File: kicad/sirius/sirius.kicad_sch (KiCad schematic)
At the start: 59 parts, among them J1 IPEX_MHF1, J2 Power In, J3 Screw_Terminal, Q1 Q_PMOS_GSD, Q2 Q_NMOS_GSD, Q3 Q_NMOS_GSD, U1 Power_Connector, U2 AP63301WU-7, U3 RFM95W-915S2, U4 LC29H (DA), U5 Pi Zero 2W

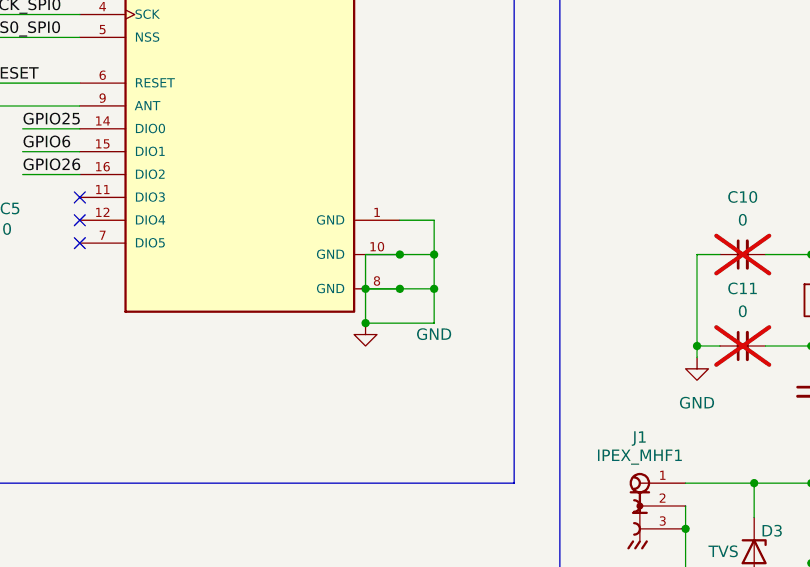
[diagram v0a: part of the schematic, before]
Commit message: Finish Sopdet schematic
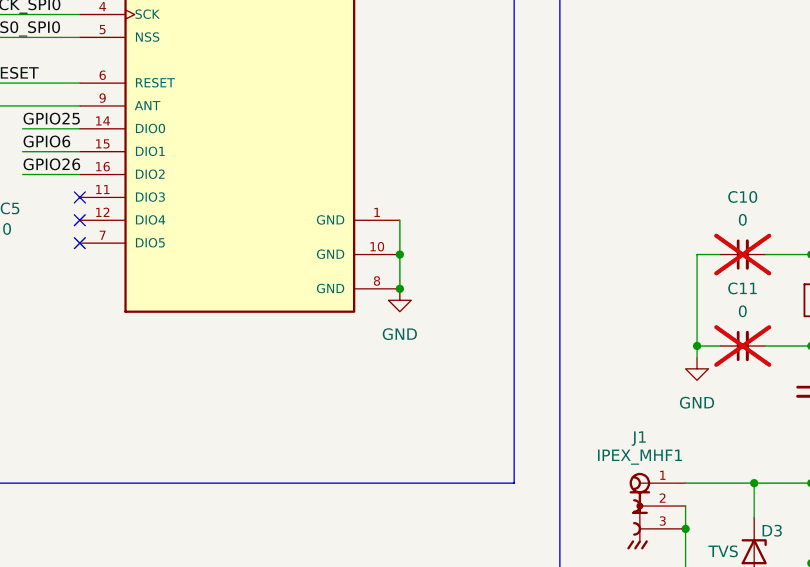
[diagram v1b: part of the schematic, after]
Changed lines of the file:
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@@
 	)
 	(junction
-		(at 74.93 184.15)
-		(diameter 0)
-		(color 0 0 0 0)
-	)
-	(junction
 		(at 196.85 198.12)
 		(diameter 0)
@@
 	)
 	(junction
-		(at 82.55 184.15)
+		(at 180.34 137.16)
 		(diameter 0)
 		(color 0 0 0 0)
 	)
 	(junction
-		(at 180.34 137.16)
+		(at 383.54 199.39)
 		(diameter 0)
 		(color 0 0 0 0)
 	)
 	(junction
-		(at 383.54 199.39)
+		(at 36.83 64.77)
 		(diameter 0)
 		(color 0 0 0 0)
 	)
 	(junction
-		(at 36.83 64.77)
+		(at 78.74 184.15)
 		(diameter 0)
 		(color 0 0 0 0)
@@
 	)
 	(junction
+		(at 78.74 180.34)
+		(diameter 0)
+		(color 0 0 0 0)
+	)
+	(junction
 		(at 375.92 135.89)
 		(diameter 0)
@@
 	)
 	(junction
-		(at 78.74 184.15)
-		(diameter 0)
-		(color 0 0 0 0)
-	)
-	(junction
-		(at 78.74 180.34)
-		(diameter 0)
-		(color 0 0 0 0)
-	)
-	(junction
 		(at 124.46 214.63)
 		(diameter 0)
@@
 	)
 	(junction
-		(at 82.55 180.34)
-		(diameter 0)
-		(color 0 0 0 0)
-	)
-	(junction
-		(at 74.93 187.96)
-		(diameter 0)
-		(color 0 0 0 0)
-	)
-	(junction
 		(at 199.39 137.16)
 		(diameter 0)
@@
 	(wire
 		(pts
-			(xy 36.83 166.37) (xy 43.18 166.37)
+			(xy 78.74 176.53) (xy 78.74 180.34)
 		)
 		(stroke
@@
 	(wire
 		(pts
-			(xy 125.73 80.01) (xy 128.27 80.01)
+			(xy 36.83 166.37) (xy 43.18 166.37)
 		)
 		(stroke
@@
 	(wire
 		(pts
-			(xy 36.83 168.91) (xy 43.18 168.91)
+			(xy 125.73 80.01) (xy 128.27 80.01)
 		)
 		(stroke
@@
 	(wire
 		(pts
-			(xy 111.76 180.34) (xy 114.3 180.34)
+			(xy 36.83 168.91) (xy 43.18 168.91)
 		)
 		(stroke
@@
 	(wire
 		(pts
-			(xy 180.34 149.86) (xy 187.96 149.86)
+			(xy 111.76 180.34) (xy 114.3 180.34)
 		)
 		(stroke
@@
 	(wire
 		(pts
-			(xy 302.26 179.07) (xy 314.96 179.07)
+			(xy 180.34 149.86) (xy 187.96 149.86)
 		)
 		(stroke
@@
 	(wire
 		(pts
-			(xy 180.34 137.16) (xy 187.96 137.16)
+			(xy 302.26 179.07) (xy 314.96 179.07)
 		)
 		(stroke
@@
 	(wire
 		(pts
-			(xy 378.46 176.53) (xy 375.92 176.53)
+			(xy 180.34 137.16) (xy 187.96 137.16)
 		)
 		(stroke
@@
 	(wire
 		(pts
-			(xy 78.74 176.53) (xy 82.55 176.53)
+			(xy 378.46 176.53) (xy 375.92 176.53)
 		)
 		(stroke
@@
 	(wire
 		(pts
-			(xy 82.55 184.15) (xy 78.74 184.15)
-		)
-		(stroke
-			(width 0)
-			(type default)
-		)
-	)
-	(wire
-		(pts
 			(xy 383.54 204.47) (xy 383.54 207.01)
 		)
@@
 	(wire
 		(pts
-			(xy 82.55 180.34) (xy 82.55 184.15)
-		)
-		(stroke
-			(width 0)
-			(type default)
-		)
-	)
-	(wire
-		(pts
 			(xy 90.17 34.29) (xy 86.36 34.29)
 		)
@@
 	(wire
 		(pts
-			(xy 194.31 205.74) (xy 196.85 205.74)
+			(xy 78.74 180.34) (xy 78.74 184.15)
 		)
 		(stroke
@@
 	(wire
 		(pts
-			(xy 250.19 194.31) (xy 254 194.31)
+			(xy 194.31 205.74) (xy 196.85 205.74)
 		)
 		(stroke
@@
 	(wire
 		(pts
-			(xy 111.76 190.5) (xy 114.3 190.5)
+			(xy 250.19 194.31) (xy 254 194.31)
 		)
 		(stroke
@@
 	(wire
 		(pts
-			(xy 199.39 157.48) (xy 199.39 165.1)
+			(xy 111.76 190.5) (xy 114.3 190.5)
 		)
 		(stroke
@@
 	(wire
 		(pts
-			(xy 119.38 190.5) (xy 124.46 190.5)
+			(xy 199.39 157.48) (xy 199.39 165.1)
 		)
 		(stroke
@@
 	(wire
 		(pts
-			(xy 110.49 205.74) (xy 118.11 205.74)
+			(xy 119.38 190.5) (xy 124.46 190.5)
 		)
 		(stroke
@@
 	(wire
 		(pts
-			(xy 90.17 38.1) (xy 93.98 38.1)
+			(xy 110.49 205.74) (xy 118.11 205.74)
 		)
 		(stroke
@@
 	(wire
 		(pts
-			(xy 238.76 208.28) (xy 243.84 208.28)
+			(xy 90.17 38.1) (xy 93.98 38.1)
 		)
 		(stroke
@@
 	(wire
 		(pts
-			(xy 74.93 184.15) (xy 74.93 187.96)
+			(xy 238.76 208.28) (xy 243.84 208.28)
 		)
 		(stroke
@@
 	(wire
 		(pts
-			(xy 82.55 187.96) (xy 74.93 187.96)
-		)
-		(stroke
-			(width 0)
-			(type default)
-		)
-	)
-	(wire
-		(pts
-			(xy 82.55 184.15) (xy 82.55 187.96)
-		)
-		(stroke
-			(width 0)
-			(type default)
-		)
-	)
-	(wire
-		(pts
 			(xy 375.92 199.39) (xy 383.54 199.39)
 		)
@@
 	(wire
 		(pts
-			(xy 74.93 180.34) (xy 74.93 184.15)
-		)
-		(stroke
-			(width 0)
-			(type default)
-		)
-	)
-	(wire
-		(pts
 			(xy 199.39 137.16) (xy 199.39 143.51)
 		)
@@
 	(wire
 		(pts
-			(xy 82.55 176.53) (xy 82.55 180.34)
-		)
-		(stroke
-			(width 0)
-			(type default)
-		)
-	)
-	(wire
-		(pts
 			(xy 199.39 149.86) (xy 199.39 157.48)
 		)
@@
 	(wire
 		(pts
-			(xy 78.74 180.34) (xy 74.93 180.34)
-		)
-		(stroke
-			(width 0)
-			(type default)
-		)
-	)
-	(wire
-		(pts
 			(xy 33.02 151.13) (xy 43.18 151.13)
 		)
@@
 	(wire
 		(pts
-			(xy 78.74 184.15) (xy 74.93 184.15)
-		)
-		(stroke
-			(width 0)
-			(type default)
-		)
-	)
-	(wire
-		(pts
-			(xy 78.74 180.34) (xy 82.55 180.34)
-		)
-		(stroke
-			(width 0)
-			(type default)
-		)
-	)
-	(wire
-		(pts
 			(xy 25.4 73.66) (xy 30.48 73.66)
 		)
@@
 	)
 	(symbol
+		(lib_id "power:GND")
+		(at 78.74 184.15 0)
+		(unit 1)
+		(body_style 1)
+		(exclude_from_sim no)
+		(in_bom yes)
+		(on_board yes)
+		(in_pos_files yes)
+		(dnp no)
+		(fields_autoplaced yes)
+		(property "Reference" "#PWR09"
+			(at 78.74 190.5 0)
+			(hide yes)
+			(show_name no)
+			(do_not_autoplace no)
+			(effects
+				(font
+					(size 1.27 1.27)
+				)
+			)
+		)
+		(property "Value" "GND"
+			(at 78.74 189.23 0)
+			(show_name no)
+			(do_not_autoplace no)
+			(effects
+				(font
+					(size 1.27 1.27)
+				)
+			)
+		)
+		(property "Footprint" ""
+			(at 78.74 184.15 0)
+			(hide yes)
+			(show_name no)
+			(do_not_autoplace no)
+			(effects
+				(font
+					(size 1.27 1.27)
+				)
+			)
+		)
+		(property "Datasheet" ""
+			(at 78.74 184.15 0)
+			(hide yes)
+			(show_name no)
+			(do_not_autoplace no)
+			(effects
+				(font
+					(size 1.27 1.27)
+				)
+			)
+		)
+		(property "Description" "Power symbol creates a global label with name \"GND\" , ground"
+			(at 78.74 184.15 0)
+			(hide yes)
+			(show_name no)
+			(do_not_autoplace no)
+			(effects
+				(font
+					(size 1.27 1.27)
+				)
+			)
+		)
+		(pin "1"
+		)
+		(instances
+			(project "sirius"
+				(path "/abc76503-1c89-48c4-92f2-dcc55eacd272"
+					(reference "#PWR09")
+					(unit 1)
+				)
+			)
+		)
+	)
+	(symbol
 		(lib_id "Transistor_FET:Q_NMOS_GSD")
 		(at 228.6 72.39 0)
@@
 					(unit 1)
 				)
-			)
-		)
-	)
-	(symbol
-		(lib_id "power:GND")
-		(at 74.93 187.96 0)
-		(unit 1)
-		(body_style 1)
-		(exclude_from_sim no)
-		(in_bom yes)
-		(on_board yes)
-		(in_pos_files yes)
-		(dnp no)
-		(property "Reference" "#PWR09"
-			(at 74.93 194.31 0)
-			(hide yes)
-			(show_name no)
-			(do_not_autoplace no)
-			(effects
-				(font
-					(size 1.27 1.27)
-				)
-			)
-		)
-		(property "Value" "GND"
-			(at 82.55 189.23 0)
-			(show_name no)
-			(do_not_autoplace no)
-			(effects
-				(font
-					(size 1.27 1.27)
-				)
-			)
-		)
-		(property "Footprint" ""
-			(at 74.93 187.96 0)
-			(hide yes)
-			(show_name no)
-			(do_not_autoplace no)
-			(effects
-				(font
-					(size 1.27 1.27)
-				)
-			)
-		)
-		(property "Datasheet" ""
-			(at 74.93 187.96 0)
-			(hide yes)
-			(show_name no)
-			(do_not_autoplace no)
-			(effects
-				(font
-					(size 1.27 1.27)
-				)
-			)
-		)
-		(property "Description" "Power symbol creates a global label with name \"GND\" , ground"
-			(at 74.93 187.96 0)
-			(hide yes)
-			(show_name no)
-			(do_not_autoplace no)
-			(effects
-				(font
-					(size 1.27 1.27)
-				)
-			)
-		)
-		(pin "1"
-		)
-		(instances
-			(project "sirius"
-				(path "/abc76503-1c89-48c4-92f2-dcc55eacd272"
-					(reference "#PWR09")
-					(unit 1)
-				)

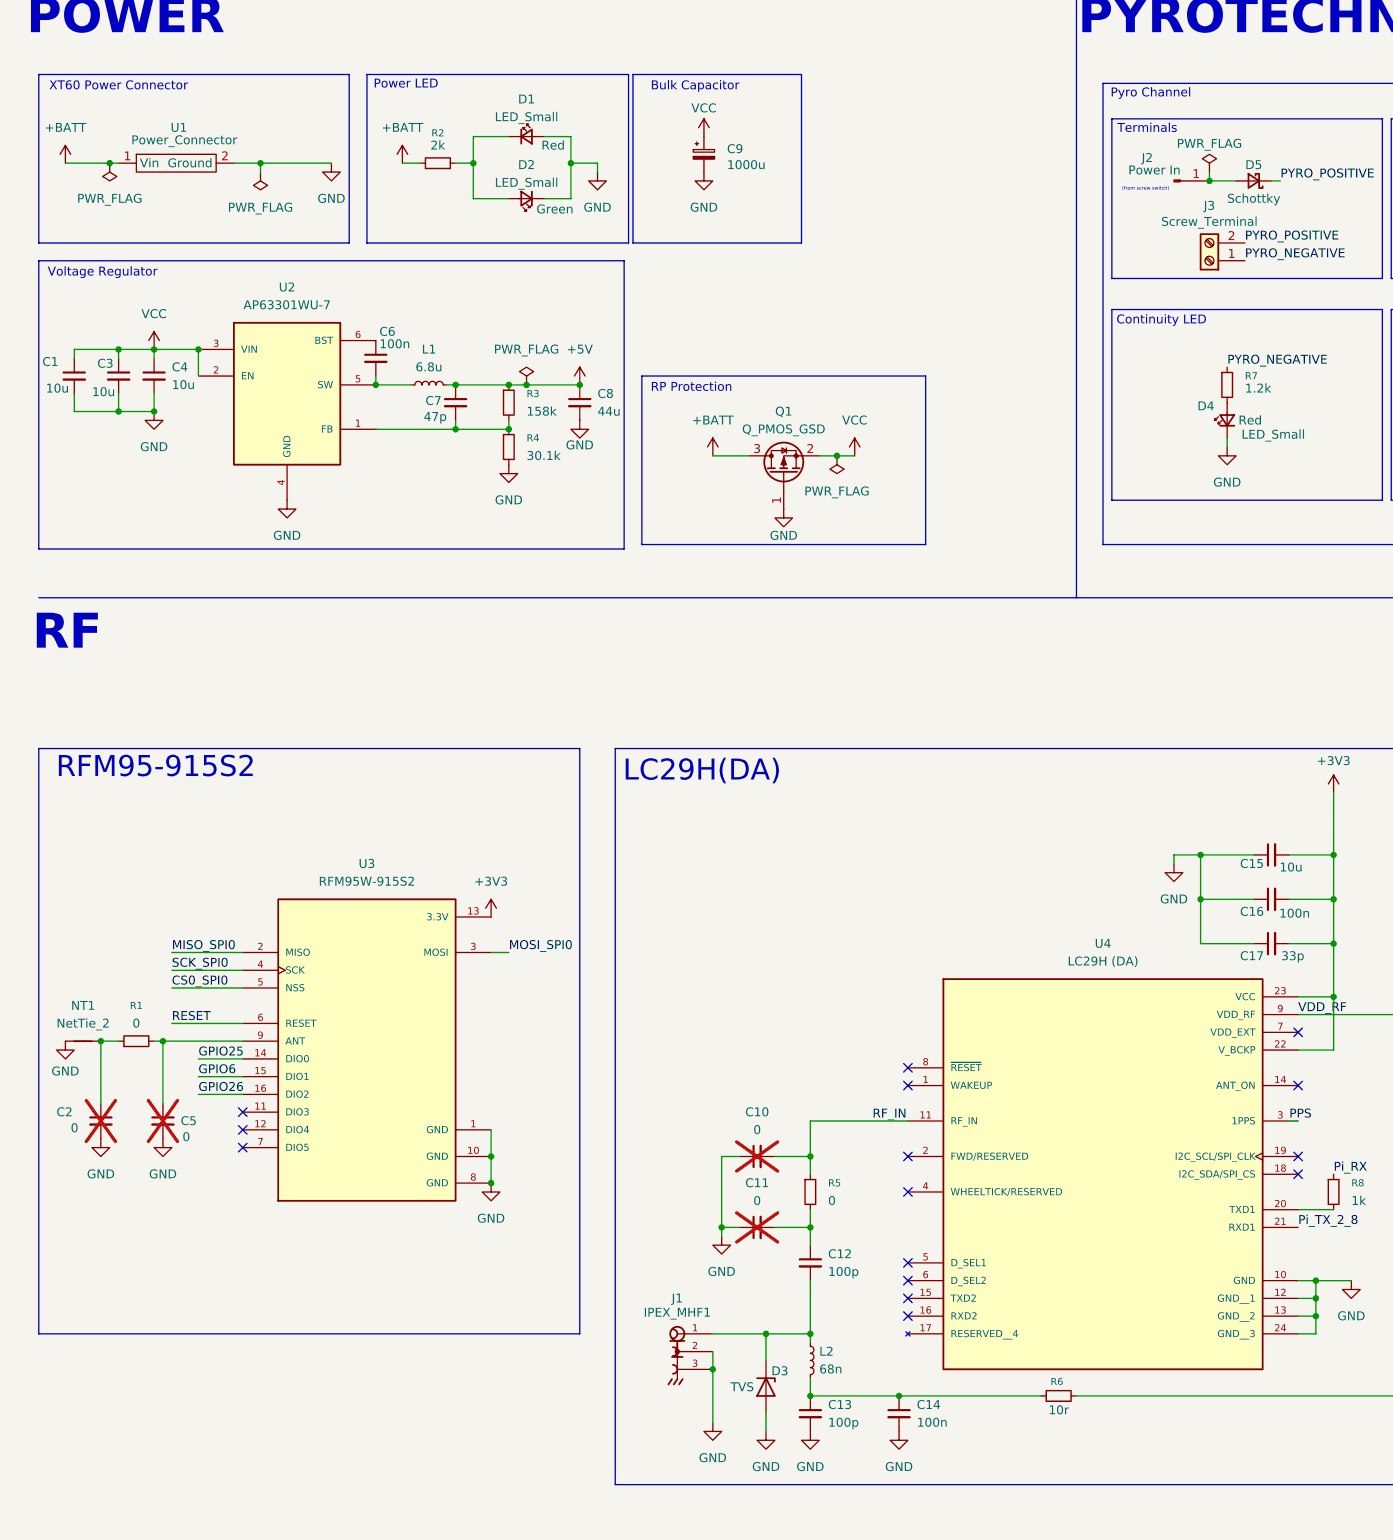
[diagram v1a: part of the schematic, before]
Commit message: Finish routing Sopdet
Logo still pending
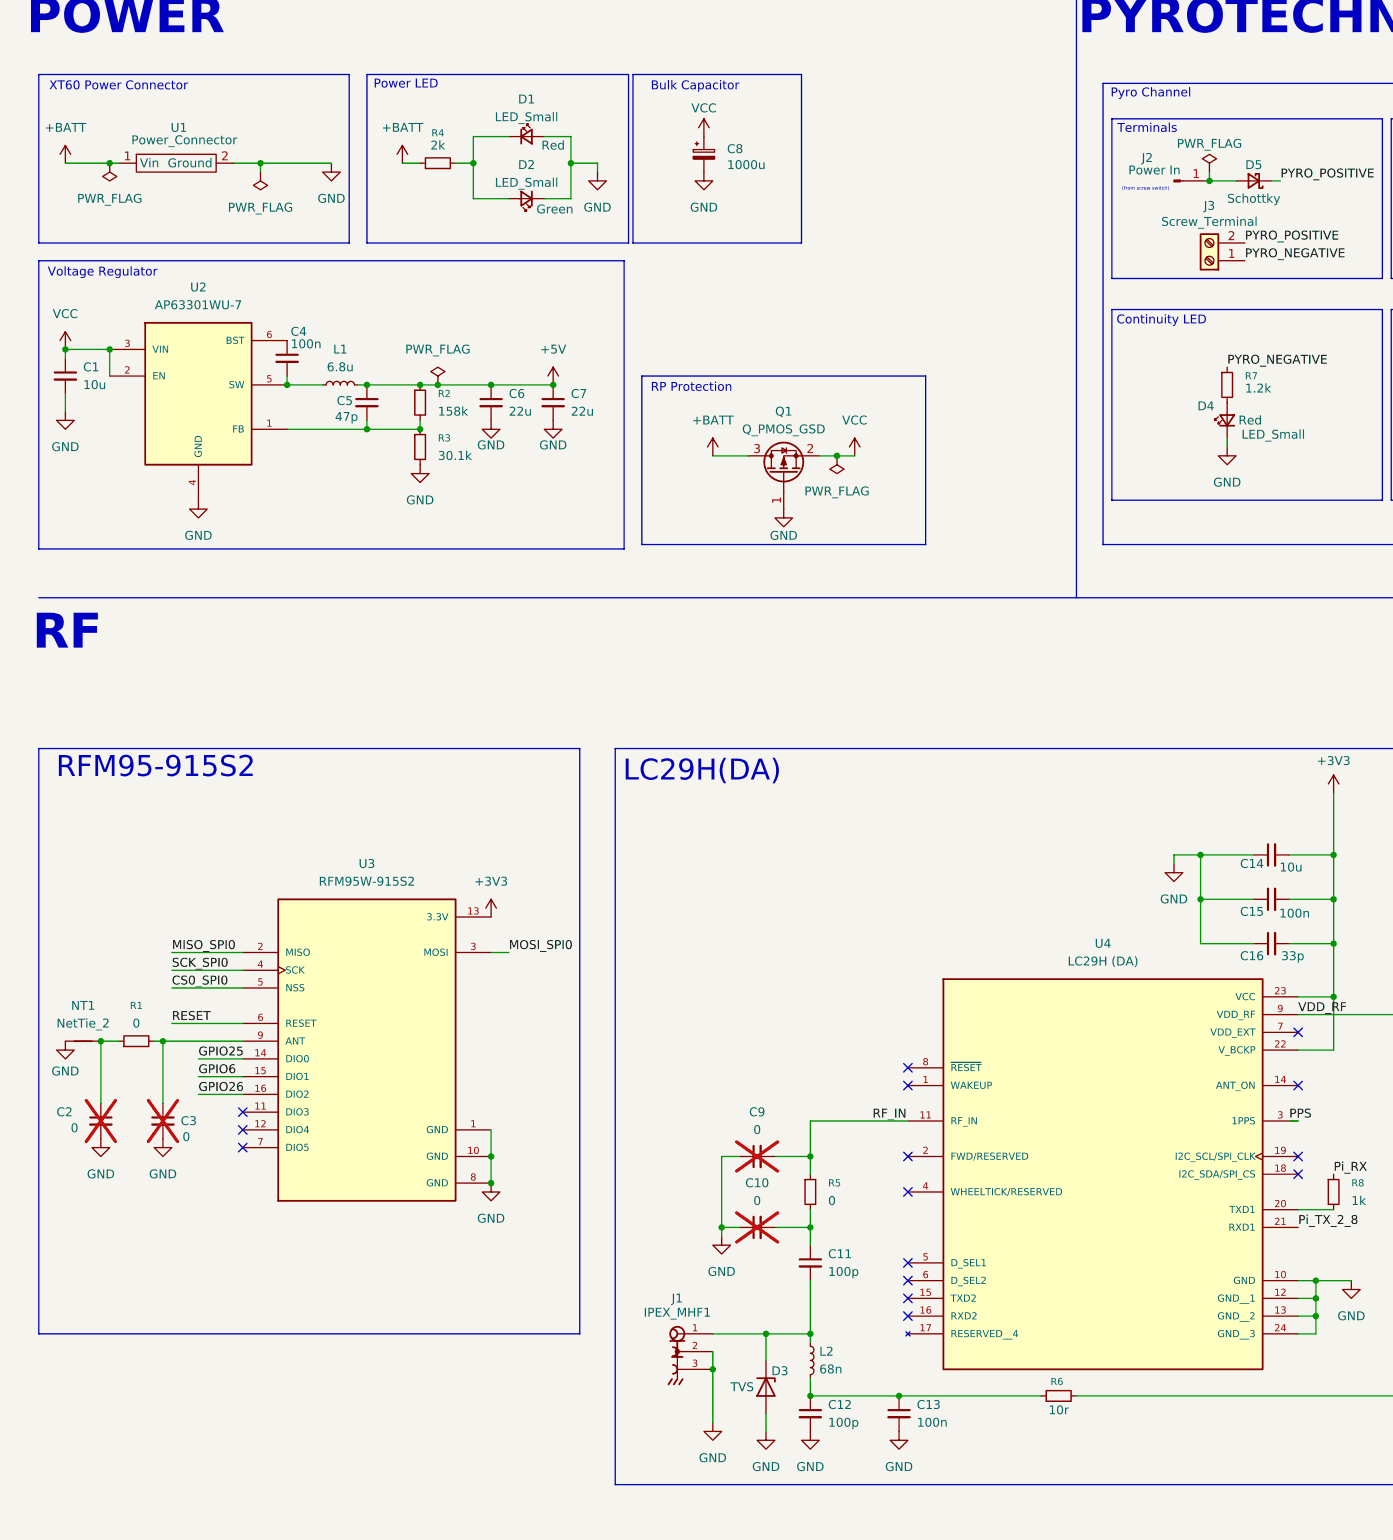
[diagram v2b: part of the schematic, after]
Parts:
- removed C1, C3: 10u, Capacitor_SMD:C_0603_1608Metric_Pad1.08x0.95mm_HandSolder, symbol Device:C_Small
- added C7: 22u, Capacitor_SMD:C_1206_3216Metric, symbol Device:C_Small
- C6: renamed from C8; value 44u -> 22u; footprint Capacitor_SMD:C_0603_1608Metric_Pad1.08x0.95mm_HandSolder -> Capacitor_SMD:C_1206_3216Metric
- renumbered C4 to C1, C11 to C10, C12 to C11, C13 to C12, C14 to C13, C15 to C14, C16 to C15, C17 to C16, C5 to C3, C6 to C4, C7 to C5, C9 to C8, C10 to C9, R3 to R2, R4 to R3, R2 to R4
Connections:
- net +5V: now also C7.1
- net GND: now also C7.2
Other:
- moved on the sheet: C1, C4, C5, C6, L1, R2, R3, U2
